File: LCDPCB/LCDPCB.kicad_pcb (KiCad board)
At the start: 2 copper layers, 23 parts, among them J1 Sockets, J2 Hot plug, J3 Programming Header, SW1 SW_Push, U1 STM32F091RCT6, U2 LD1117S12TR_SOT223

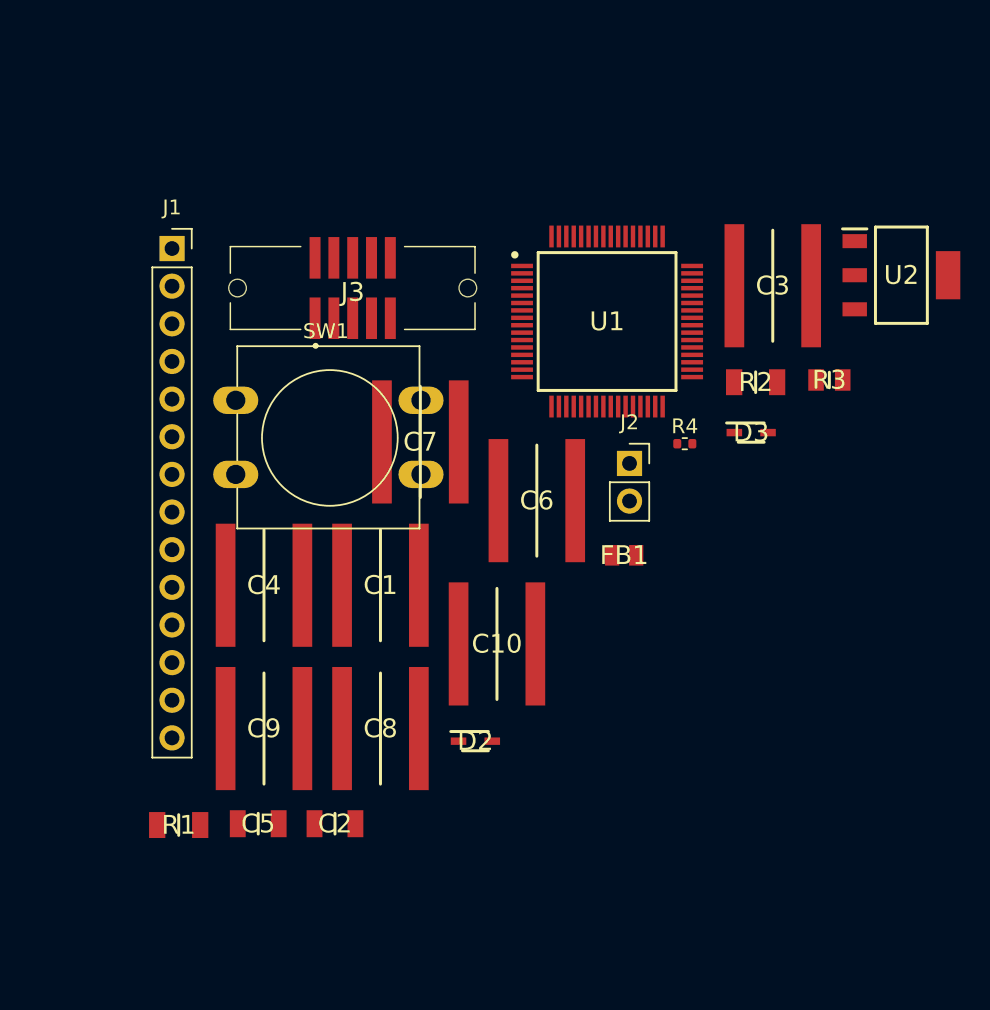
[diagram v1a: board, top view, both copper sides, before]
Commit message: updated with pins
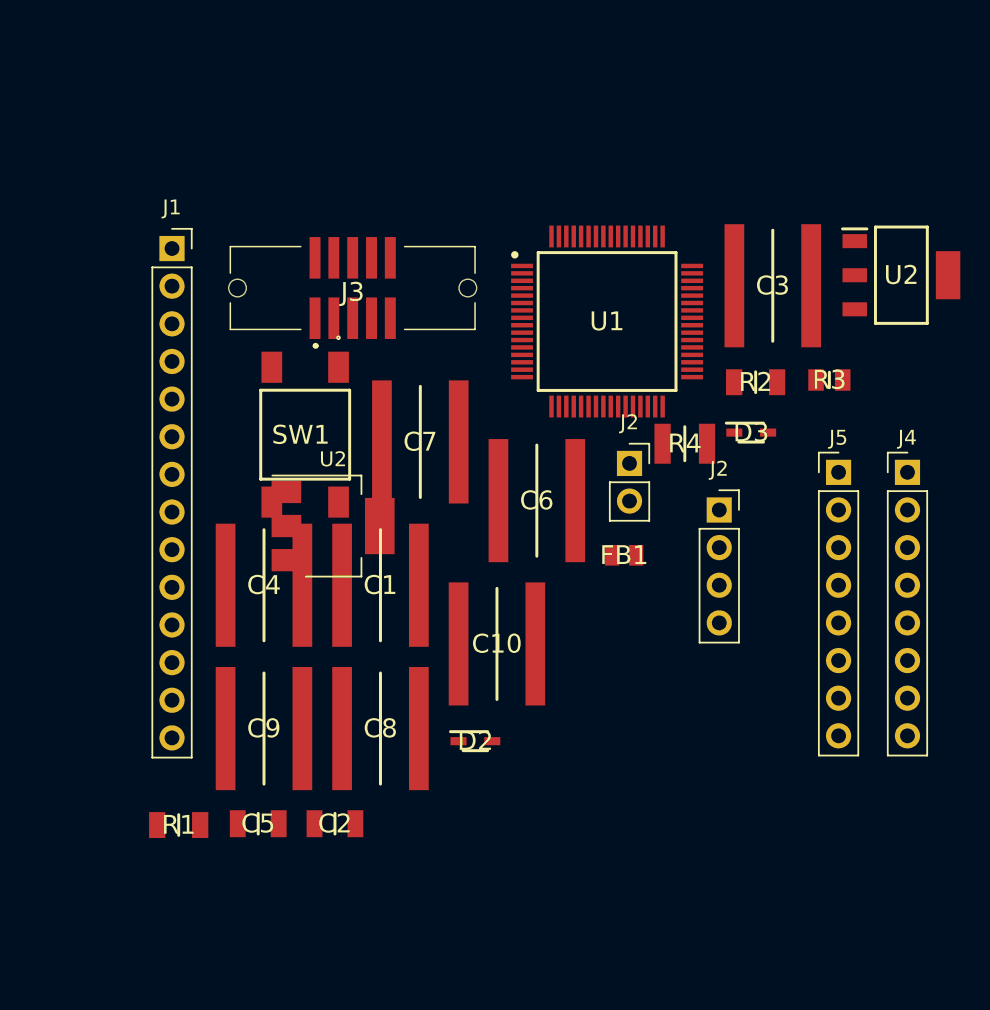
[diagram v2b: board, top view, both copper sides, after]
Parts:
- added J2: Hot Plug, Connector_PinSocket_2.54mm:PinSocket_1x04_P2.54mm_Vertical, F.Cu at (157.5, 86.4)
- added J4: Conn_01x08_Male, Connector_PinHeader_2.54mm:PinHeader_1x08_P2.54mm_Vertical, F.Cu at (170.2, 83.8)
- added J5: Conn_01x08_Male, Connector_PinHeader_2.54mm:PinHeader_1x08_P2.54mm_Vertical, F.Cu at (165.5, 83.8)
- added U2: LD1117S12TR_SOT223, Package_TO_SOT_SMD:SOT-223-3_TabPin2, F.Cu at (131.4, 87.4)
- D2: value BAT60A -> BAT60JFLIM; footprint lib_file:BAT60B -> lib_file:BAT60JFILM
- D3: value BAT60A -> BAT60JFILM; footprint lib_file:BAT60B -> lib_file:BAT60JFILM
- R4: footprint Resistor_SMD:R_0402_1005Metric -> lib_file:5.1kR
- SW1: footprint Button_Switch_THT:SW_PUSH-12mm -> lib_file:Button
- moved SW1 5.23 mm to (129.5, 81.3)
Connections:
- net /BOOT0 renamed PF11
- net /PA13 renamed PA13
- net /PA14 renamed PA14
- C2 pad 1: Net-(U2-Pad3) -> Net-(C2-Pad1)
- C3 pad 1: Net-(U2-Pad3) -> Net-(C2-Pad1)
- C4 pad 1: Net-(C5-Pad1) -> Net-(C4-Pad1)
- C5 pad 1: Net-(C5-Pad1) -> Net-(C4-Pad1)
- D2 pad 2: Net-(C5-Pad1) -> Net-(C4-Pad1)
- J1 pad 9: unconnected-(J1-Pad9) -> PB4
- U1 pad 56: unconnected-(U1-Pad56) -> PB4

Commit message: display done
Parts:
- removed the J2 at (151.4, 83.2)
- removed the J2 at (157.5, 86.4)
- removed the U2 at (131.4, 87.4)
- removed the U2 at (169.8, 70.5)
- added H1: MountingHole, MountingHole:MountingHole_2.2mm_M2_ISO7380, F.Cu at (168.0, 57.0)
- added H2: MountingHole, MountingHole:MountingHole_2.2mm_M2_ISO7380, F.Cu at (168.0, 115.0)
- added H3: MountingHole, MountingHole:MountingHole_2.2mm_M2_ISO7380, F.Cu at (114.0, 57.0)
- added H4: MountingHole, MountingHole:MountingHole_2.2mm_M2_ISO7380, F.Cu at (114.0, 115.0)
- added J2: Hot Plug, Connector_PinSocket_2.54mm:PinSocket_1x04_P2.54mm_Vertical, F.Cu at (114.3, 77.5)
- added U2: LD1117S12TR_SOT223, Package_TO_SOT_SMD:SOT-223-3_TabPin2, F.Cu at (116.5, 69.8)
- C1, C10, C3, C4, C6, C7, C8, C9: footprint lib_file:.1uFC -> lib_file:CAPC3225X88N
- moved J4 56.4 mm to (114.3, 91.4)
- moved C2 46.6 mm to (121.0, 62.1), turned to 180 degrees
- moved C9 46.3 mm to (164.1, 73.7), turned to -90 degrees
- moved J1 42.7 mm to (157.5, 90.2), turned to -90 degrees
- moved C8 37.4 mm to (160.0, 73.7), turned to -90 degrees
- moved C5 36.5 mm to (129.2, 71.1), turned to -90 degrees
- moved D2 36.0 mm to (131.2, 67.3), turned to 180 degrees
- moved C3 36.0 mm to (125.5, 66.0), turned to -90 degrees
- moved C10 33.6 mm to (168.1, 73.7), turned to -90 degrees
- moved R3 33.1 mm to (132.5, 71.1), turned to -90 degrees
- moved R1 32.3 mm to (133.1, 77.7), turned to 90 degrees
- moved R2 22.8 mm to (139.7, 67.3)
- moved C7 20.6 mm to (156.2, 73.7), turned to -90 degrees
- moved C4 20.4 mm to (125.6, 71.1), turned to -90 degrees
- moved FB1 19.6 mm to (154.4, 70.1), turned to 180 degrees
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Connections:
- C10 pad 1: Net-(C10-Pad1) -> +3V0
- C7 pad 1: Net-(C10-Pad1) -> +3V0
- C8 pad 1: Net-(C10-Pad1) -> +3V0
- C9 pad 1: Net-(C10-Pad1) -> +3V0
- FB1 pad 1: Net-(C10-Pad1) -> +3V0
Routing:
- net +3V0: track 0.00 -> 134.1 mm, vias 0 -> 6
- net PA13: track 0.00 -> 91.7 mm, vias 0 -> 3
- net PA14: track 0.00 -> 79.7 mm, vias 0 -> 2
- net PB4: track 0.00 -> 58.4 mm, vias 0 -> 4
- net GND: track 0.00 -> 56.7 mm, vias 0 -> 14
- net PB5: track 0.00 -> 54.8 mm, vias 0 -> 6
- net NRST: track 0.00 -> 54.5 mm, vias 0 -> 4
- net PB3: track 0.00 -> 48.4 mm, vias 0 -> 6
- net PF11: track 0.00 -> 45.5 mm
- net PB8: track 0.00 -> 45.3 mm, vias 0 -> 4
- net PB14: track 0.00 -> 41.8 mm, vias 0 -> 2
- net PA6: track 0.00 -> 24.8 mm
- net PB11: track 0.00 -> 23.6 mm
- net PA7: track 0.00 -> 20.4 mm
- net Net-(C4-Pad1): track 0.00 -> 18.7 mm
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- added copper zone on B.Cu, net GND
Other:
- board outline added: 60 x 64 mm

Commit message: design mk 2
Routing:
- net PA7: track 20.4 -> 57.5 mm, vias 0 -> 6
- net PA6: track 24.8 -> 52.8 mm, vias 0 -> 4
- net PB11: track 23.6 -> 36.0 mm, vias 0 -> 2
- net +3V0: track 134.1 -> 143.5 mm, vias 6 -> 8

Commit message: v2 lcd pcb
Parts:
- added R5: 10, lib_file:10R, F.Cu at (118.2, 80.0)
- added R6: 10, lib_file:10R, F.Cu at (118.1, 82.5)
- C1, C3, C4: footprint lib_file:CAPC3225X88N -> lib_file:.1uF
- C10, C6, C7, C8, C9: footprint lib_file:CAPC3225X88N -> lib_file:.1uF; moved to B.Cu
- C5: footprint lib_file:22uFC -> lib_file:22uF
- FB1: moved to B.Cu
- J3: footprint lib_file:programming header -> Connector_PinSocket_2.54mm:PinSocket_2x05_P2.54mm_Vertical
- R1, R2: footprint lib_file:100KR -> lib_file:100k
- R3: footprint lib_file:1kR -> lib_file:1k
- R4: footprint lib_file:5.1kR -> lib_file:5.1k
- moved SW1 38.3 mm to (162.3, 79.8), turned to 180 degrees
- moved C8 29.4 mm to (137.7, 92.8), turned to 180 degrees
- moved C9 27.5 mm to (144.3, 92.8), turned to 180 degrees
- moved C7 25.6 mm to (132.7, 83.7)
- moved C1 25.3 mm to (157.5, 78.8)
- moved R1 21.7 mm to (154.8, 79.0)
- moved C10 20.4 mm to (149.0, 80.9)
- moved FB1 18.7 mm to (136.7, 76.0), turned to 90 degrees
- moved C6 13.4 mm to (139.3, 76.6), turned to 180 degrees
- moved D3 9.72 mm to (144.1, 66.8), turned to 180 degrees
- moved R4 9.21 mm to (148.6, 66.8), turned to 0 degrees
- moved J1 8.89 mm to (157.5, 99.1)
- moved U1 8.61 mm to (140.8, 84.7)
- moved J3 5.38 mm to (135.9, 58.4), turned to 90 degrees
- moved D2 2.77 mm to (130.7, 70.0)
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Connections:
- C2 pad 1: Net-(C2-Pad1) -> +5V
- C3 pad 1: Net-(C2-Pad1) -> +5V
- J2 pad 2: PA6 -> Net-(J2-Pad2)
- J2 pad 3: PA7 -> Net-(J2-Pad3)
- J3 pad 7: /V3.3_IN -> unconnected-(J3-Pad7)
- J3 pad 8: /V3.3_IN -> unconnected-(J3-Pad8)
- U1 pad 13: +3.3VA -> +3.3V
- U2 pad 3: Net-(C2-Pad1) -> +5V
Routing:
- net +3V0: track 143.5 -> 25.3 mm
- net NRST: track 54.5 -> 82.1 mm, vias 4 -> 5
- net +5V: track 5.09 -> 30.8 mm, vias 0 -> 2
- net +3.3V: track 0.00 -> 25.4 mm, vias 0 -> 2
- net PA13: track 91.7 -> 68.1 mm
- net PA14: track 79.7 -> 64.5 mm
- net GND: track 56.7 -> 41.9 mm
- net PA7: track 57.5 -> 44.1 mm, vias 6 -> 2
- net Net-(C2-Pad1): track 11.3 -> 0.00 mm
- net PB3: track 48.4 -> 57.7 mm, vias 6 -> 2
- net PB5: track 54.8 -> 48.5 mm, vias 6 -> 3
- net PA6: track 52.8 -> 47.0 mm, vias 4 -> 2
- net PB14: track 41.8 -> 36.9 mm
- net PB4: track 58.4 -> 62.8 mm, vias 4 -> 2
- net Net-(C4-Pad1): track 18.7 -> 14.3 mm
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- added copper zone on F.Cu, net +3V0

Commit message: minor
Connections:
- C4 pad 1: Net-(C4-Pad1) -> +3.3V
- C5 pad 1: Net-(C4-Pad1) -> +3.3V
- D2 pad 2: Net-(C4-Pad1) -> +3.3V
- U2 pad 2: Net-(C4-Pad1) -> +3.3V
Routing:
- net +3.3V: track 25.4 -> 49.3 mm
- net Net-(C4-Pad1): track 14.3 -> 0.00 mm
- net PB3: track 57.7 -> 57.9 mm, vias 2 -> 4

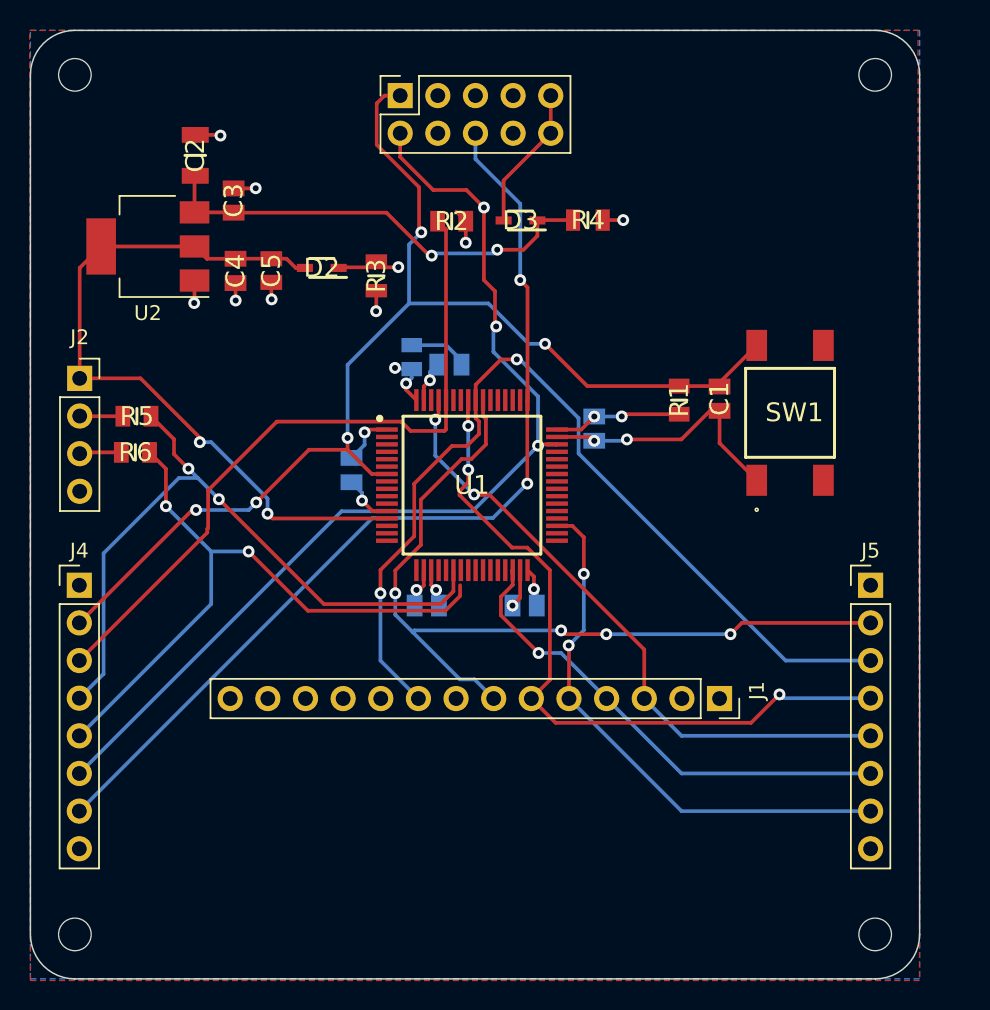
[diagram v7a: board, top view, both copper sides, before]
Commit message: added thermal relief, made 5V routes wider
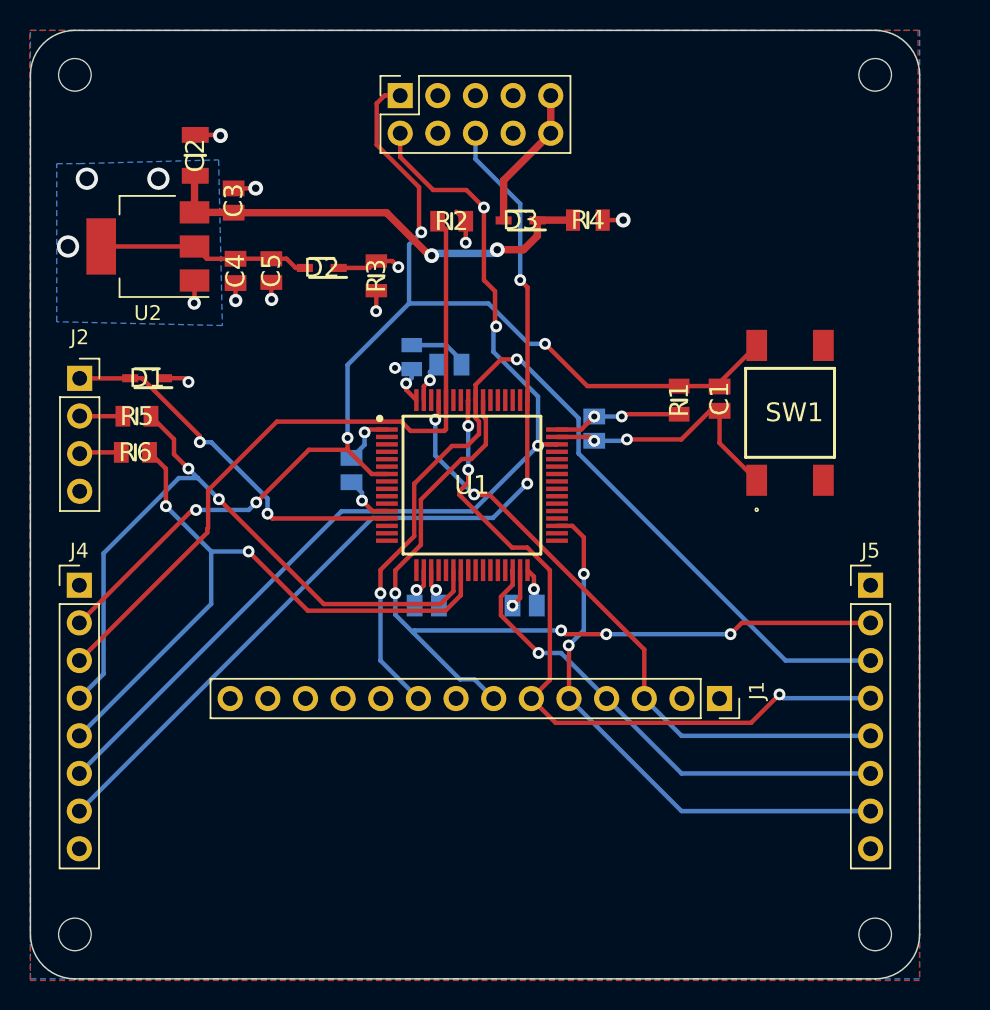
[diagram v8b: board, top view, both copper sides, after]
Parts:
- added D1: BAT60JFLIM, lib_file:BAT60JFILM, F.Cu at (118.9, 77.5)
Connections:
- C4 pad 1: +3.3V -> Net-(C4-Pad1)
- C5 pad 1: +3.3V -> Net-(C4-Pad1)
- D2 pad 2: +3.3V -> Net-(C4-Pad1)
- U2 pad 2: +3.3V -> Net-(C4-Pad1)
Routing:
- net +3.3V: track 49.3 -> 25.5 mm
- net Net-(C4-Pad1): track 0.00 -> 14.3 mm
- net +3V0: track 25.3 -> 27.5 mm, vias 8 -> 9
- net PA7: track 44.1 -> 45.2 mm
- net (no net): vias 0 -> 3
- added copper zone on B.Cu, net (none)
